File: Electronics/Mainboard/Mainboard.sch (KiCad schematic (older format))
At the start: 2 parts, among them J1 Raspberry_Pi_2_3

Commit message: Supply board and tunneling amp finished
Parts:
- removed J1: Raspberry_Pi_2_3, Connector_PinHeader_2.54mm:PinHeader_2x20_P2.54mm_Horizontal, symbol Connector:Raspberry_Pi_2_3
- removed JP1: SolderJumper_2_Bridged, Jumper:SolderJumper-2_P1.3mm_Bridged_Pad1.0x1.5mm, symbol Jumper:SolderJumper_2_Bridged
- added A1: Pololu_Breakout_A4988, Module:Pololu_Breakout-16_15.2x20.3mm, symbol Driver_Motor:Pololu_Breakout_A4988
- added J2: DB25_Male_MountingHoles, Connector_Dsub:DSUB-25_Female_Horizontal_P2.77x2.84mm_EdgePinOffset4.94mm_Housed_MountingHolesOffset7.48mm, symbol Connector:DB25_Male_MountingHoles
- added N1: Housing, STM_Custom_Lib:Hammond_1455L1601, symbol Mechanical:Housing
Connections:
- net labels removed: GND
- wire segments 16 -> 0
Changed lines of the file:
@@
 EESchema Schematic File Version 4
+LIBS:Mainboard-cache
 EELAYER 30 0
 EELAYER END
@@
 Comment4 ""
 $EndDescr
-$Comp
-L Connector:Raspberry_Pi_2_3 J1
-U 1 1 5D616137
-P 2600 2700
-F 0 "J1" H 2600 4181 50  0000 C CNN
-F 1 "Raspberry_Pi_2_3" H 2600 4090 50  0000 C CNN
-F 2 "Connector_PinHeader_2.54mm:PinHeader_2x20_P2.54mm_Horizontal" H 2600 2700 50  0001 C CNN
-F 3 "https://www.raspberrypi.org/documentation/hardware/raspberrypi/schematics/rpi_SCH_3bplus_1p0_reduced.pdf" H 2600 2700 50  0001 C CNN
-	1    2600 2700
-	1    0    0    -1
-$EndComp
-Wire Wire Line
-	2200 4000 2200 4100
-Wire Wire Line
-	2200 4100 2300 4100
-Wire Wire Line
-	2900 4100 2900 4000
-Wire Wire Line
-	2800 4000 2800 4100
-Connection ~ 2800 4100
-Wire Wire Line
-	2800 4100 2900 4100
-Wire Wire Line
-	2700 4100 2700 4000
-Connection ~ 2700 4100
-Wire Wire Line
-	2700 4100 2800 4100
-Wire Wire Line
-	2600 4000 2600 4100
-Connection ~ 2600 4100
-Wire Wire Line
-	2600 4100 2700 4100
-Wire Wire Line
-	2500 4100 2500 4000
-Connection ~ 2500 4100
-Wire Wire Line
-	2500 4100 2600 4100
-Wire Wire Line
-	2400 4000 2400 4100
-Connection ~ 2400 4100
-Wire Wire Line
-	2400 4100 2500 4100
-Wire Wire Line
-	2300 4100 2300 4000
-Connection ~ 2300 4100
-Wire Wire Line
-	2300 4100 2400 4100
-Wire Wire Line
-	2200 4100 2200 4200
-Connection ~ 2200 4100
-$Comp
-L power:GND #PWR01
-U 1 1 5D618EE8
-P 2200 4200
-F 0 "#PWR01" H 2200 3950 50  0001 C CNN
-F 1 "GND" H 2205 4027 50  0000 C CNN
-F 2 "" H 2200 4200 50  0001 C CNN
-F 3 "" H 2200 4200 50  0001 C CNN
-	1    2200 4200
-	1    0    0    -1
-$EndComp
-$Comp
-L Jumper:SolderJumper_2_Bridged JP1
-U 1 1 5D61A3F4
-P 3700 1800
-F 0 "JP1" H 3700 2005 50  0000 C CNN
-F 1 "SolderJumper_2_Bridged" H 3700 1914 50  0000 C CNN
-F 2 "Jumper:SolderJumper-2_P1.3mm_Bridged_Pad1.0x1.5mm" H 3700 1800 50  0001 C CNN
-F 3 "~" H 3700 1800 50  0001 C CNN
-	1    3700 1800
-	1    0    0    -1
-$EndComp
 $Sheet
 S 8700 3500 1100 600
@@
 F1 "DAC.sch" 50
 $EndSheet
+$Comp
+L Mechanical:Housing N1
+U 1 1 5D85575A
+P 9950 1450
+F 0 "N1" H 10103 1484 50  0000 L CNN
+F 1 "Housing" H 10103 1393 50  0000 L CNN
+F 2 "STM_Custom_Lib:Hammond_1455L1601" H 10000 1500 50  0001 C CNN
+F 3 "~" H 10000 1500 50  0001 C CNN
+	1    9950 1450
+	1    0    0    -1
+$EndComp
+$Comp
+L Connector:DB25_Male_MountingHoles J2
+U 1 1 5D869ED2
+P 1550 2500
+F 0 "J2" H 1468 3992 50  0000 C CNN
+F 1 "DB25_Male_MountingHoles" H 1468 3901 50  0000 C CNN
+F 2 "Connector_Dsub:DSUB-25_Female_Horizontal_P2.77x2.84mm_EdgePinOffset4.94mm_Housed_MountingHolesOffset7.48mm" H 1550 2500 50  0001 C CNN
+F 3 " ~" H 1550 2500 50  0001 C CNN
+	1    1550 2500
+	-1   0    0    -1
+$EndComp
+$Comp
+L Driver_Motor:Pololu_Breakout_A4988 A1
+U 1 1 5D86EADE
+P 5200 2900
+F 0 "A1" H 5250 3781 50  0000 C CNN
+F 1 "Pololu_Breakout_A4988" H 5250 3690 50  0000 C CNN
+F 2 "Module:Pololu_Breakout-16_15.2x20.3mm" H 5475 2150 50  0001 L CNN
+F 3 "https://www.pololu.com/product/2980/pictures" H 5300 2600 50  0001 C CNN
+	1    5200 2900
+	1    0    0    -1
+$EndComp
 $EndSCHEMATC

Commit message: Many changes. I lost track of them...
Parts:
- removed A1: Pololu_Breakout_A4988, Module:Pololu_Breakout-16_15.2x20.3mm, symbol Driver_Motor:Pololu_Breakout_A4988
- added J1, J7: Conn_Coaxial, STM_Custom_Lib:SMA_horizontal, symbol Connector:Conn_Coaxial
- added J3, J4: 609-5192-ND, STM_Custom_Lib:DSUB-9_Amphenol_LD09S33E4GV00LF, symbol Connector:DB9_Female_MountingHoles
- added U14: LM75C, Package_SO:SOIC-8_3.9x4.9mm_P1.27mm, symbol Sensor_Temperature:LM75C
- J2: footprint Connector_Dsub:DSUB-25_Female_Horizontal_P2.77x2.84mm_EdgePinOffset4.94mm_Housed_MountingHolesOffset7.48mm -> Connector_Dsub:DSUB-25_Male_Horizontal_P2.77x2.84mm_EdgePinOffset4.94mm_Housed_MountingHolesOffset7.48mm
- N1: footprint STM_Custom_Lib:Hammond_1455L1601 -> STM_Custom_Lib:Hammond_1455P1601
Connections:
- net labels added: GNDA
- wire segments 0 -> 84
- no-connect marks 0 -> 1
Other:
- note added: "TODO: Analog Volotage on connector for preamp..."
- moved on the sheet: J2

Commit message: Layout of piezo DACs ready
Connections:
- net labels added: +15V, +20V, -15V, -20V, 3V3, 9V, GND
- wire segments 84 -> 95
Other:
- moved on the sheet: J1, J3, J7, N1, U14

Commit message: ADC Schematic
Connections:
- net labels added: Bias, CLK, MISO, MOSI, REF_N, REF_P, ~CS-Bias, ~CS-X, ~CS-Y, ~CS-Z, ~LDAC
- wire segments 95 -> 132
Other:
- moved on the sheet: J3

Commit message: Reference schematic
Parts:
- removed J1, J7: Conn_Coaxial, STM_Custom_Lib:SMA_horizontal, symbol Connector:Conn_Coaxial
- added J1: 609-5192-ND, STM_Custom_Lib:DSUB-9_Amphenol_LD09S33E4GV00LF, symbol Connector:DB9_Female_MountingHoles
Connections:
- net labels added: ADC_BUSY, ADC_CLK, ADC_CONV, ADC_IN+, ADC_IN-, ADC_MISO, ADC_MOSI, DAC_CLK, DAC_MISO, DAC_MOSI, ~DAC_CS-Bias, ~DAC_CS-X, ~DAC_CS-Y, ~DAC_CS-Z, ~DAC_LDAC
- net labels removed: CLK, GNDA, MISO, MOSI, ~CS-Bias, ~CS-X, ~CS-Y, ~CS-Z, ~LDAC
- wire segments 132 -> 169
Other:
- moved on the sheet: J3, J4

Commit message: Reference layout finished
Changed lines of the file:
@@
 F7 "VDD" I L 4600 6050 50
 F8 "VMOT" I L 4600 5950 50
+F9 "~ENABLE" I L 4600 6350 50
+F10 "STEP" I L 4600 6450 50
+F11 "DIR" I L 4600 6550 50
 $EndSheet
 $Comp
@@
 Wire Wire Line
 	1750 3200 2150 3200
+Text Label 4500 6050 2    50   ~ 0
+3V3
 $EndSCHEMATC

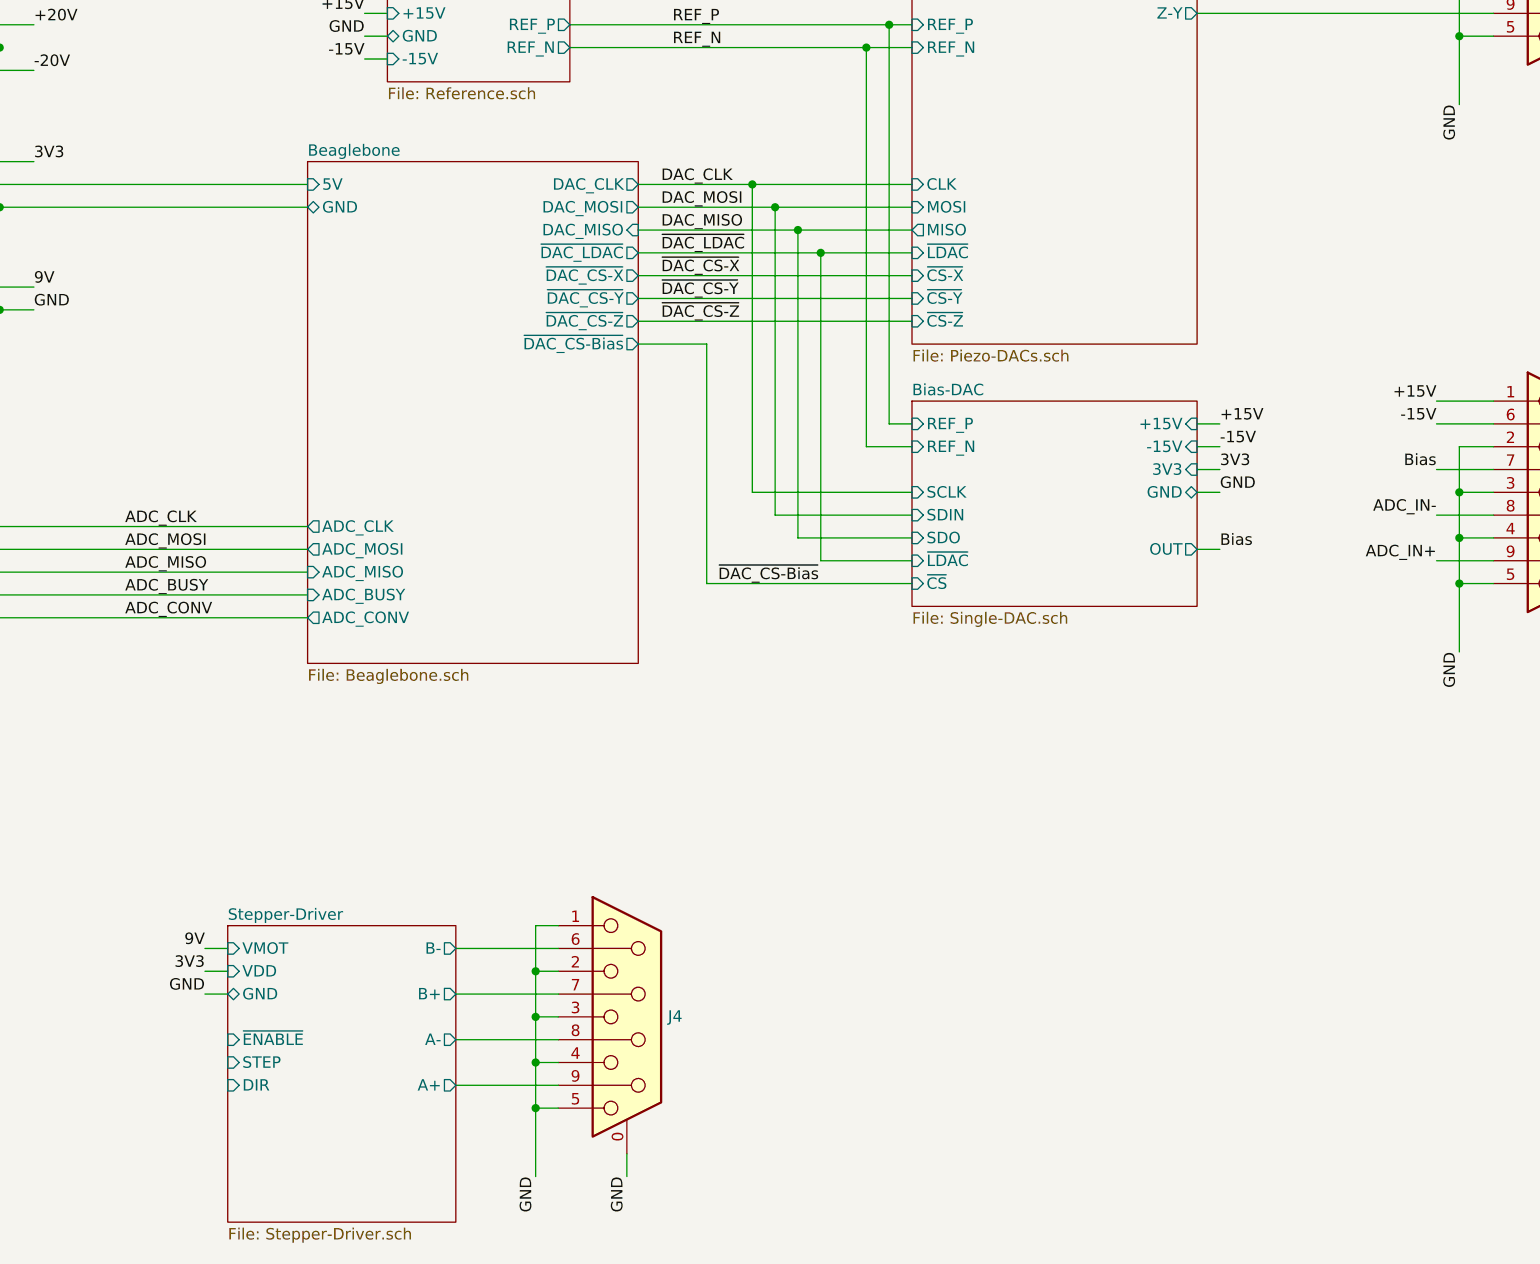
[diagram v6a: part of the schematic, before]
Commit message: SPI Connections finished
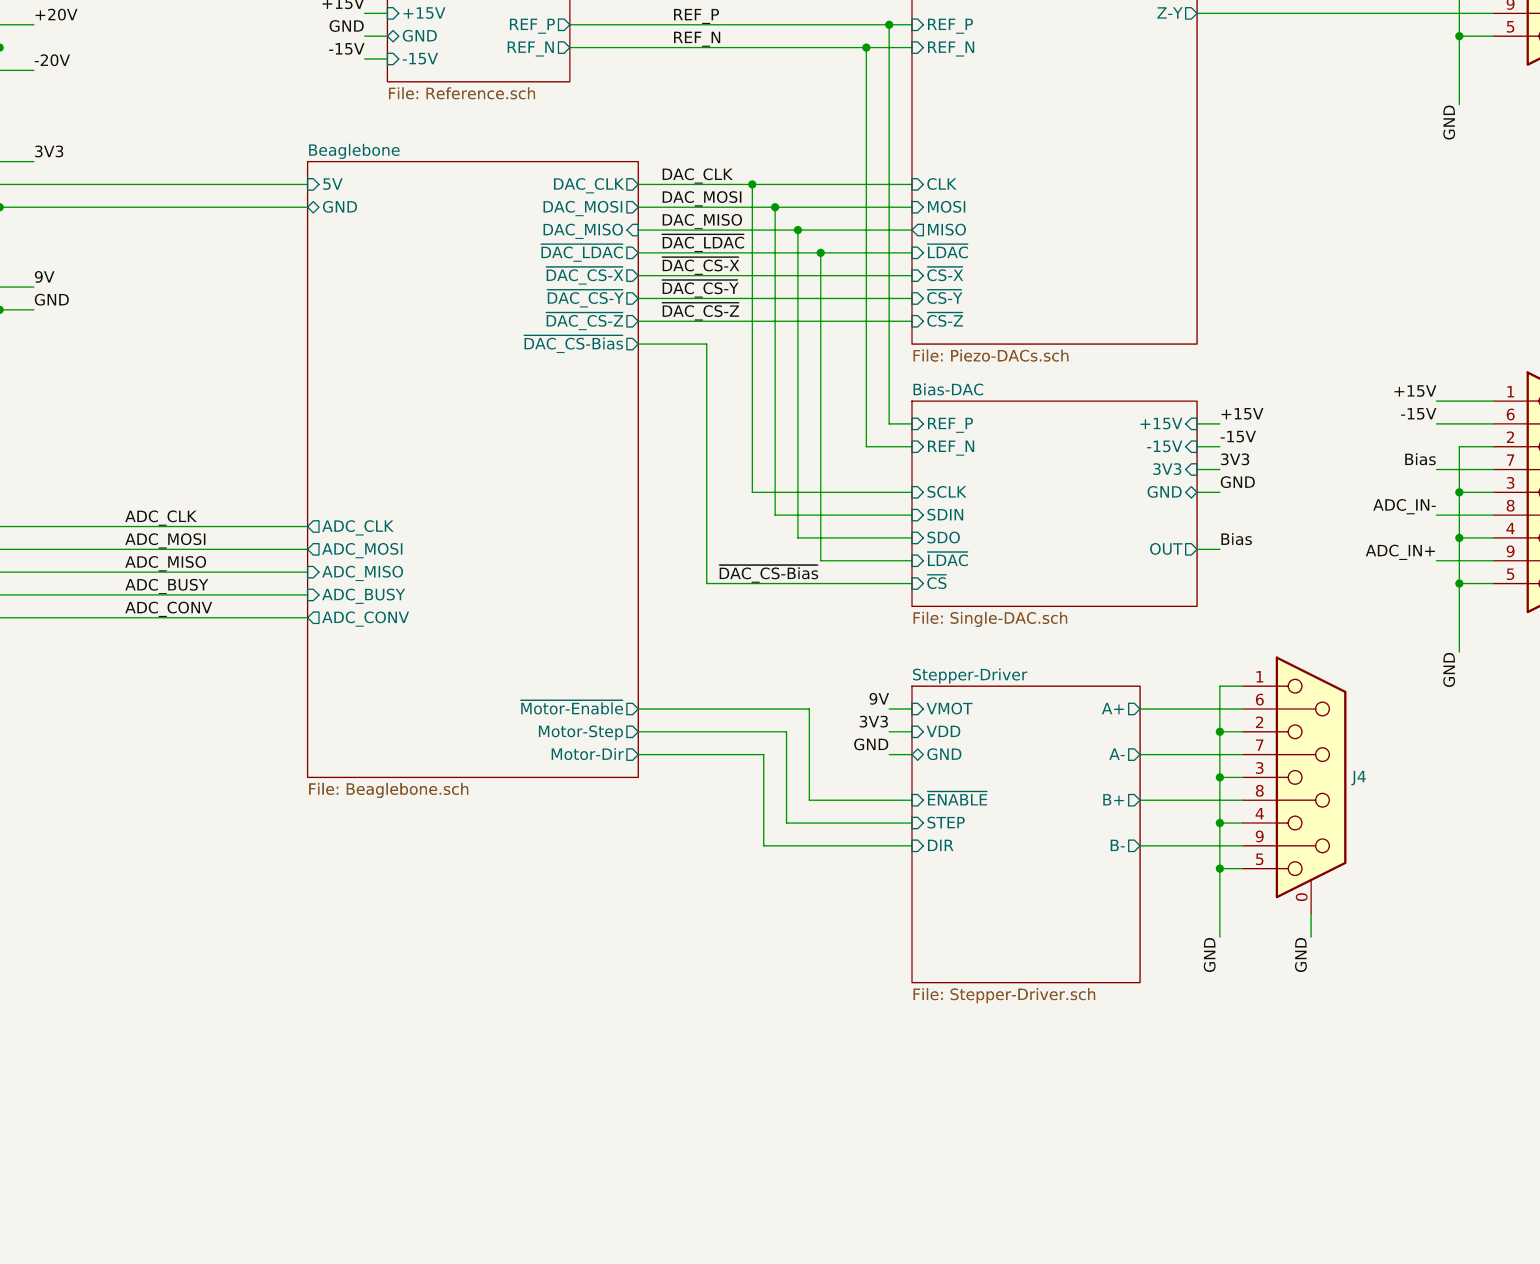
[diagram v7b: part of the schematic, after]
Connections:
- net Stepper-Driver/A+: now also J4.6; no longer J4.9
- net Stepper-Driver/A-: now also J4.7; no longer J4.8
- net Stepper-Driver/B+: now also J4.8; no longer J4.7
- net Stepper-Driver/B-: now also J4.9; no longer J4.6
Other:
- moved on the sheet: J4
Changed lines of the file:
@@
 	10000 1350 10000 1550
 $Sheet
-S 4950 2500 1450 2200
+S 4950 2500 1450 2700
 U 5ECB043D
 F0 "Beaglebone" 50
@@
 F15 "ADC_BUSY" I L 4950 4400 50
 F16 "ADC_CONV" O L 4950 4500 50
+F17 "~Motor-Enable" O R 6400 4900 50
+F18 "Motor-Dir" O R 6400 5100 50
+F19 "Motor-Step" O R 6400 5000 50
 $EndSheet
 Wire Wire Line
@@
 Connection ~ 1750 3200
 $Sheet
-S 4600 5850 1000 1300
+S 7600 4800 1000 1300
 U 5ED2FDF6
 F0 "Stepper-Driver" 50
 F1 "Stepper-Driver.sch" 50
-F2 "A+" O R 5600 6550 50
-F3 "A-" O R 5600 6350 50
-F4 "B+" O R 5600 6150 50
-F5 "B-" O R 5600 5950 50
-F6 "GND" B L 4600 6150 50
-F7 "VDD" I L 4600 6050 50
-F8 "VMOT" I L 4600 5950 50
-F9 "~ENABLE" I L 4600 6350 50
-F10 "STEP" I L 4600 6450 50
-F11 "DIR" I L 4600 6550 50
+F2 "A+" O R 8600 4900 50
+F3 "A-" O R 8600 5100 50
+F4 "B+" O R 8600 5300 50
+F5 "B-" O R 8600 5500 50
+F6 "GND" B L 7600 5100 50
+F7 "VDD" I L 7600 5000 50
+F8 "VMOT" I L 7600 4900 50
+F9 "~ENABLE" I L 7600 5300 50
+F10 "STEP" I L 7600 5400 50
+F11 "DIR" I L 7600 5500 50
 $EndSheet
 $Comp
 L Connector:DB9_Female_MountingHoles J4
 U 1 1 5EB434D0
-P 6350 6250
-F 0 "J4" H 6530 6252 50  0000 L CNN
-F 1 "609-5192-ND " H 6530 6161 50  0001 L CNN
-F 2 "STM_Custom_Lib:DSUB-9_Amphenol_LD09S33E4GV00LF" H 6350 6250 50  0001 C CNN
-F 3 " ~" H 6350 6250 50  0001 C CNN
-F 4 "609-5192-ND " H 6350 6250 50  0001 C CNN "Digikey"
-	1    6350 6250
+P 9350 5200
+F 0 "J4" H 9530 5202 50  0000 L CNN
+F 1 "609-5192-ND " H 9530 5111 50  0001 L CNN
+F 2 "STM_Custom_Lib:DSUB-9_Amphenol_LD09S33E4GV00LF" H 9350 5200 50  0001 C CNN
+F 3 " ~" H 9350 5200 50  0001 C CNN
+F 4 "609-5192-ND " H 9350 5200 50  0001 C CNN "Digikey"
+	1    9350 5200
 	1    0    0    -1
 $EndComp
@@
 GND
 Wire Wire Line
-	6050 6650 5950 6650
-Wire Wire Line
-	5950 6650 5950 6450
-Wire Wire Line
-	5950 6450 6050 6450
-Wire Wire Line
-	6050 6250 5950 6250
-Wire Wire Line
-	5950 6250 5950 6450
-Connection ~ 5950 6450
-Wire Wire Line
-	5950 6250 5950 6050
-Wire Wire Line
-	5950 6050 6050 6050
-Connection ~ 5950 6250
-Wire Wire Line
-	5950 6050 5950 5850
-Wire Wire Line
-	5950 5850 6050 5850
-Connection ~ 5950 6050
-Wire Wire Line
-	5600 5950 6050 5950
-Wire Wire Line
-	5600 6150 6050 6150
-Wire Wire Line
-	5600 6350 6050 6350
-Wire Wire Line
-	5600 6550 6050 6550
-Wire Wire Line
-	5950 6650 5950 6950
-Connection ~ 5950 6650
-Text Label 6350 6950 3    50   ~ 0
-GND
-Text Label 5950 6950 3    50   ~ 0
-GND
-Wire Wire Line
-	6350 6950 6350 6850
+	9050 5600 8950 5600
+Wire Wire Line
+	8950 5600 8950 5400
+Wire Wire Line
+	8950 5400 9050 5400
+Wire Wire Line
+	9050 5200 8950 5200
+Wire Wire Line
+	8950 5200 8950 5400
+Connection ~ 8950 5400
+Wire Wire Line
+	8950 5200 8950 5000
+Wire Wire Line
+	8950 5000 9050 5000
+Connection ~ 8950 5200
+Wire Wire Line
+	8950 5000 8950 4800
+Wire Wire Line
+	8950 4800 9050 4800
+Connection ~ 8950 5000
+Wire Wire Line
+	8600 4900 9050 4900
+Wire Wire Line
+	8600 5100 9050 5100
+Wire Wire Line
+	8600 5300 9050 5300
+Wire Wire Line
+	8600 5500 9050 5500
+Wire Wire Line
+	8950 5600 8950 5900
+Connection ~ 8950 5600
+Text Label 9350 5900 3    50   ~ 0
+GND
+Text Label 8950 5900 3    50   ~ 0
+GND
+Wire Wire Line
+	9350 5900 9350 5800
 Wire Wire Line
 	3600 2700 4950 2700
@@
 	3500 2600 4950 2600
 Wire Wire Line
-	4600 6150 4500 6150
-Wire Wire Line
-	4500 6050 4600 6050
-Wire Wire Line
-	4600 5950 4500 5950
-Text Label 4500 6150 2    50   ~ 0
-GND
-Text Label 4500 5950 2    50   ~ 0
+	7600 5100 7500 5100
+Wire Wire Line
+	7500 5000 7600 5000
+Wire Wire Line
+	7600 4900 7500 4900
+Text Label 7500 5100 2    50   ~ 0
+GND
+Text Label 7500 4900 2    50   ~ 0
 9V
 Wire Wire Line
@@
 Wire Wire Line
 	1750 3200 2150 3200
-Text Label 4500 6050 2    50   ~ 0
+Text Label 7500 5000 2    50   ~ 0
 3V3
+Wire Wire Line
+	6400 4900 7150 4900
+Wire Wire Line
+	7150 4900 7150 5300
+Wire Wire Line
+	7150 5300 7600 5300
+Wire Wire Line
+	7600 5400 7050 5400
+Wire Wire Line
+	7050 5400 7050 5000
+Wire Wire Line
+	7050 5000 6400 5000
+Wire Wire Line
+	6400 5100 6950 5100
+Wire Wire Line
+	6950 5100 6950 5500
+Wire Wire Line
+	6950 5500 7600 5500
 $EndSCHEMATC

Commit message: Further layout stuff
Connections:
- net +15V: now also J1.6; no longer J1.1
- net -15V: now also J1.1; no longer J1.6
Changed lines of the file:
@@
 Wire Wire Line
 	10150 4250 9900 4250
+Text Label 9900 3650 2    50   ~ 0
++15V
 Text Label 9900 3550 2    50   ~ 0
-+15V
-Text Label 9900 3650 2    50   ~ 0
 -15V
 Text Label 9900 3850 2    50   ~ 0
